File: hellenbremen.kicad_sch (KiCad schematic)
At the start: 5 parts

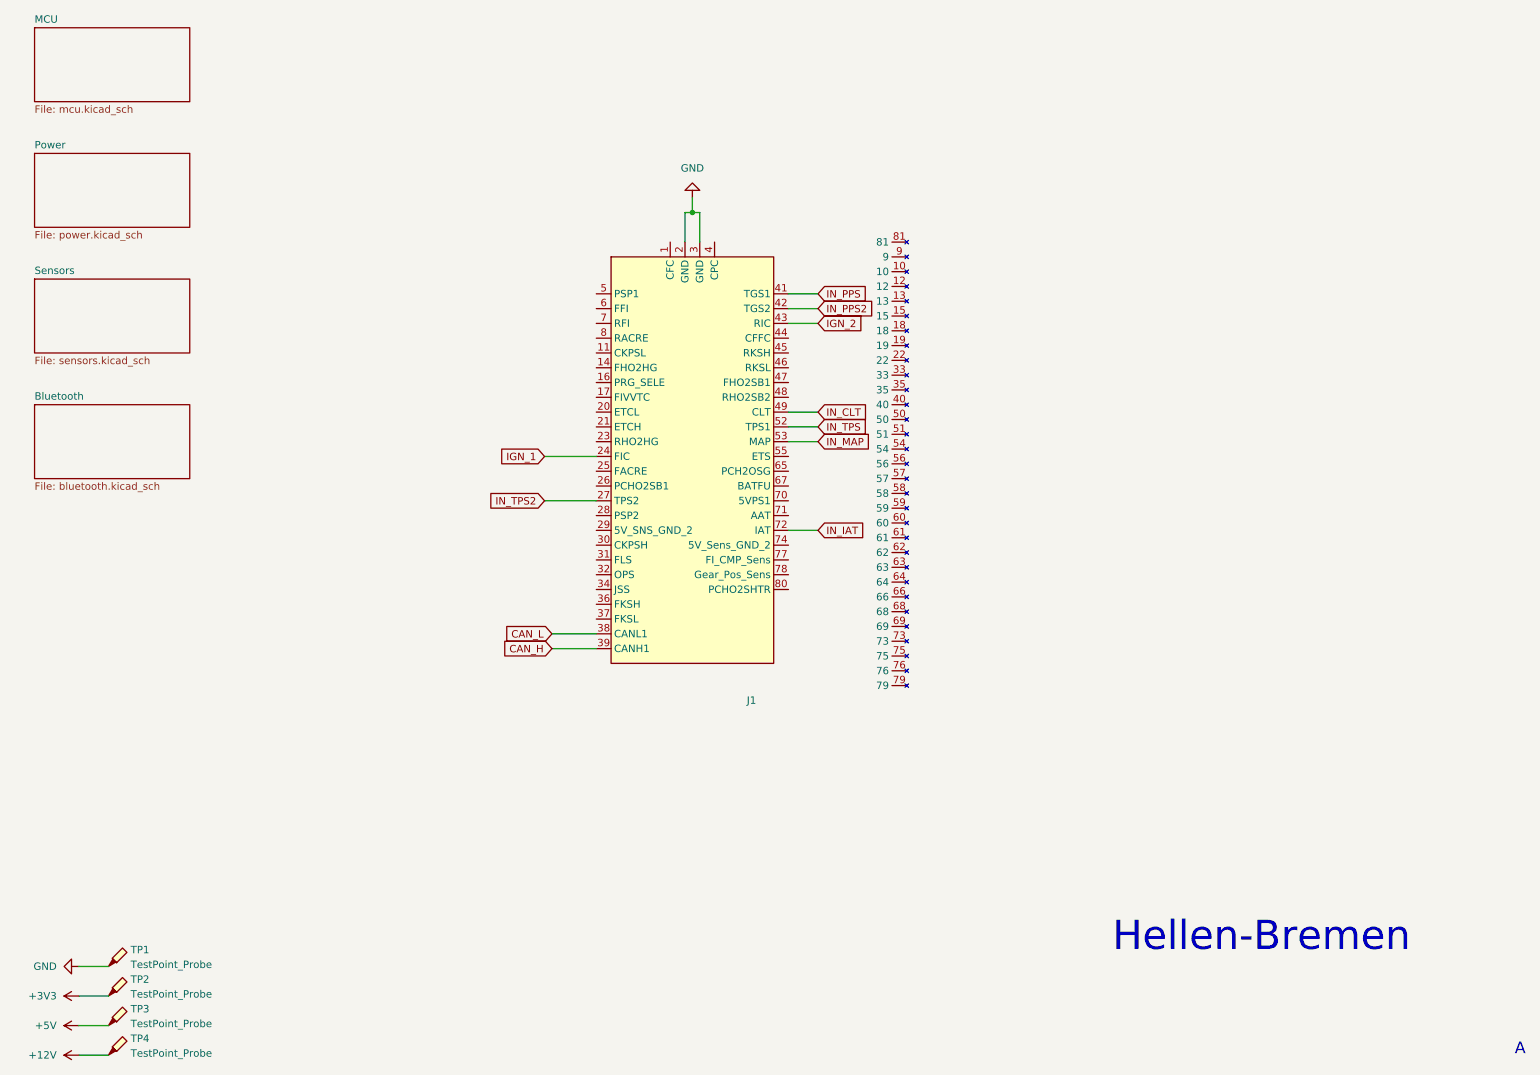
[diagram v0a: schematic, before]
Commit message: Implementing some inputs and outputs
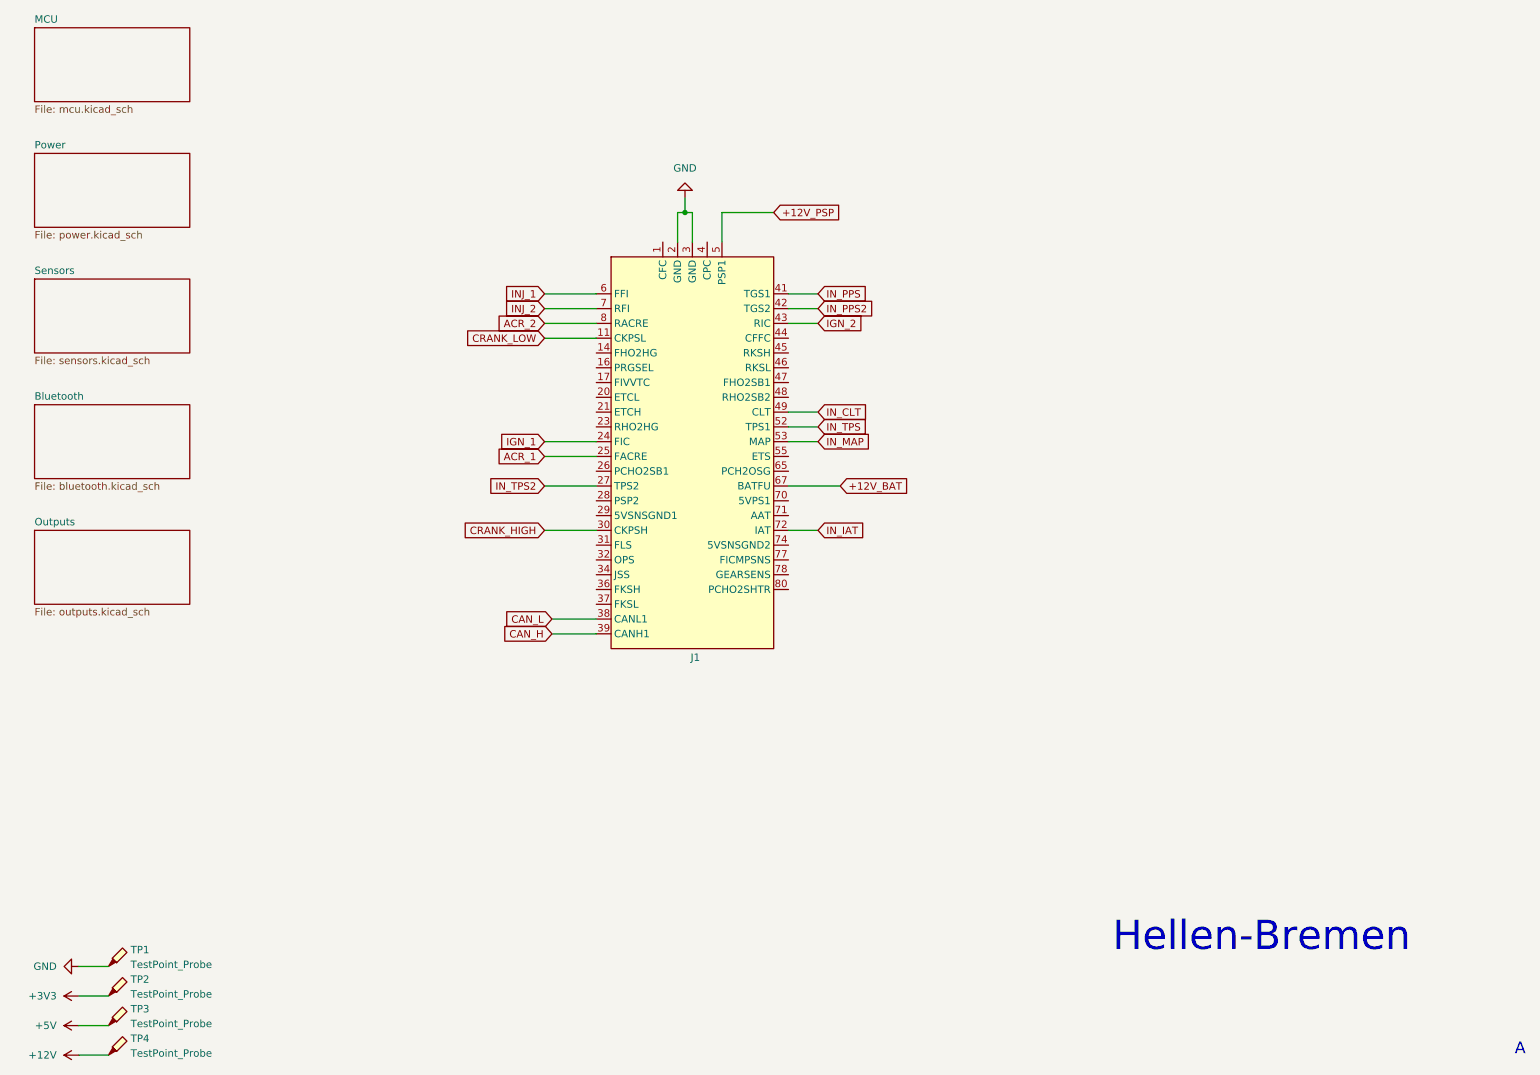
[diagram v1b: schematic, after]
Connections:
- net CRANK_LOW: now reaches J1.11 (CKPSL)
- net ACR_1: now reaches J1.25 (FACRE)
- net CRANK_HIGH: now reaches J1.30 (CKPSH)
- net +12V_PSP: now reaches J1.5 (PSP1)
- net INJ_1: now reaches J1.6 (FFI)
- net +12V_BAT: now reaches J1.67 (BATFU)
- net INJ_2: now reaches J1.7 (RFI)
- net ACR_2: now reaches J1.8 (RACRE)
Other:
- added sheet Outputs (outputs.kicad_sch)

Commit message: still initial layout
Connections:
- net GND: now also J1.29 (5VSNSGND1), J1.74 (5VSNSGND2)
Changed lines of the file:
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@@
 	(wire
 		(pts
-			(xy 144.78 104.14) (xy 149.86 104.14)
+			(xy 144.78 104.14) (xy 153.67 104.14)
 		)
 		(stroke
@@
 	(wire
 		(pts
-			(xy 144.78 63.5) (xy 149.86 63.5)
+			(xy 144.78 63.5) (xy 153.67 63.5)
 		)
 		(stroke
@@
 	(wire
 		(pts
-			(xy 144.78 83.82) (xy 149.86 83.82)
+			(xy 148.59 106.68) (xy 144.78 106.68)
+		)
+		(stroke
+			(width 0)
+			(type default)
+		)
+	)
+	(wire
+		(pts
+			(xy 144.78 83.82) (xy 153.67 83.82)
 		)
 		(stroke
@@
 	(wire
 		(pts
-			(xy 144.78 68.58) (xy 149.86 68.58)
-		)
-		(stroke
-			(width 0)
-			(type default)
-		)
-	)
-	(wire
-		(pts
-			(xy 144.78 88.9) (xy 149.86 88.9)
+			(xy 107.95 101.6) (xy 111.76 101.6)
+		)
+		(stroke
+			(width 0)
+			(type default)
+		)
+	)
+	(wire
+		(pts
+			(xy 144.78 68.58) (xy 153.67 68.58)
+		)
+		(stroke
+			(width 0)
+			(type default)
+		)
+	)
+	(wire
+		(pts
+			(xy 144.78 88.9) (xy 153.67 88.9)
 		)
 		(stroke
@@
 	(wire
 		(pts
-			(xy 144.78 66.04) (xy 149.86 66.04)
-		)
-		(stroke
-			(width 0)
-			(type default)
-		)
-	)
-	(wire
-		(pts
-			(xy 144.78 86.36) (xy 149.86 86.36)
+			(xy 144.78 66.04) (xy 153.67 66.04)
+		)
+		(stroke
+			(width 0)
+			(type default)
+		)
+	)
+	(wire
+		(pts
+			(xy 144.78 86.36) (xy 153.67 86.36)
 		)
 		(stroke
@@
 	(global_label "IN_PPS2"
 		(shape input)
-		(at 149.86 66.04 0)
+		(at 153.67 66.04 0)
 		(fields_autoplaced yes)
 		(effects
@@
 		)
 		(property "Intersheetrefs" "${INTERSHEET_REFS}"
-			(at 160.7071 66.04 0)
+			(at 164.5171 66.04 0)
 			(effects
 				(font
@@
 	(global_label "IN_PPS"
 		(shape input)
-		(at 149.86 63.5 0)
+		(at 153.67 63.5 0)
 		(fields_autoplaced yes)
 		(effects
@@
 		)
 		(property "Intersheetrefs" "${INTERSHEET_REFS}"
-			(at 159.4976 63.5 0)
+			(at 163.3076 63.5 0)
 			(effects
 				(font
@@
 	(global_label "IGN_2"
 		(shape input)
-		(at 149.86 68.58 0)
+		(at 153.67 68.58 0)
 		(fields_autoplaced yes)
 		(effects
@@
 		)
 		(property "Intersheetrefs" "${INTERSHEET_REFS}"
-			(at 158.2276 68.58 0)
+			(at 162.0376 68.58 0)
 			(effects
 				(font
@@
 	(global_label "IN_TPS"
 		(shape input)
-		(at 149.86 86.36 0)
+		(at 153.67 86.36 0)
 		(fields_autoplaced yes)
 		(effects
@@
 		)
 		(property "Intersheetrefs" "${INTERSHEET_REFS}"
-			(at 159.1952 86.36 0)
+			(at 163.0052 86.36 0)
 			(effects
 				(font
@@
 	(global_label "IN_CLT"
 		(shape input)
-		(at 149.86 83.82 0)
+		(at 153.67 83.82 0)
 		(fields_autoplaced yes)
 		(effects
@@
 		)
 		(property "Intersheetrefs" "${INTERSHEET_REFS}"
-			(at 159.0138 83.82 0)
+			(at 162.8238 83.82 0)
 			(effects
 				(font
@@
 	(global_label "IN_IAT"
 		(shape input)
-		(at 149.86 104.14 0)
+		(at 153.67 104.14 0)
 		(fields_autoplaced yes)
 		(effects
@@
 		)
 		(property "Intersheetrefs" "${INTERSHEET_REFS}"
-			(at 158.4091 104.14 0)
+			(at 162.2191 104.14 0)
 			(effects
 				(font
@@
 	(global_label "IN_MAP"
 		(shape input)
-		(at 149.86 88.9 0)
+		(at 153.67 88.9 0)
 		(fields_autoplaced yes)
 		(effects
@@
 		)
 		(property "Intersheetrefs" "${INTERSHEET_REFS}"
-			(at 159.5581 88.9 0)
+			(at 163.3681 88.9 0)
 			(effects
 				(font
@@
 	(symbol
 		(lib_id "power:GND")
+		(at 148.59 106.68 90)
+		(unit 1)
+		(exclude_from_sim no)
+		(in_bom yes)
+		(on_board yes)
+		(dnp no)
+		(fields_autoplaced yes)
+		(property "Reference" "#PWR039"
+			(at 154.94 106.68 0)
+			(effects
+				(font
+					(size 1.27 1.27)
+				)
+				(hide yes)
+			)
+		)
+		(property "Value" "GND"
+			(at 152.4 106.6801 90)
+			(effects
+				(font
+					(size 1.27 1.27)
+				)
+				(justify right)
+			)
+		)
+		(property "Footprint" ""
+			(at 148.59 106.68 0)
+			(effects
+				(font
+					(size 1.27 1.27)
+				)
+				(hide yes)
+			)
+		)
+		(property "Datasheet" ""
+			(at 148.59 106.68 0)
+			(effects
+				(font
+					(size 1.27 1.27)
+				)
+				(hide yes)
+			)
+		)
+		(property "Description" "Power symbol creates a global label with name \"GND\" , ground"
+			(at 148.59 106.68 0)
+			(effects
+				(font
+					(size 1.27 1.27)
+				)
+				(hide yes)
+			)
+		)
+		(pin "1"
+		)
+		(instances
+			(project "hellenbremen"
+				(path "/83409e39-90d0-4c85-be2e-bd292bea7c12"
+					(reference "#PWR039")
+					(unit 1)
+				)
+			)
+		)
+	)
+	(symbol
+		(lib_id "power:GND")
 		(at 22.86 179.07 270)
 		(unit 1)
@@
 					(unit 1)
 				)
+			)
+		)
+	)
+	(symbol
+		(lib_id "power:GND")
+		(at 107.95 101.6 270)
+		(unit 1)
+		(exclude_from_sim no)
+		(in_bom yes)
+		(on_board yes)
+		(dnp no)
+		(fields_autoplaced yes)
+		(property "Reference" "#PWR038"
+			(at 101.6 101.6 0)
+			(effects
+				(font
+					(size 1.27 1.27)
+				)
+				(hide yes)
+			)
+		)
+		(property "Value" "GND"
+			(at 104.14 101.5999 90)
+			(effects
+				(font
+					(size 1.27 1.27)
+				)
+				(justify right)
+			)
+		)
+		(property "Footprint" ""
+			(at 107.95 101.6 0)
+			(effects
+				(font
+					(size 1.27 1.27)
+				)
+				(hide yes)
+			)
+		)
+		(property "Datasheet" ""
+			(at 107.95 101.6 0)
+			(effects
+				(font
+					(size 1.27 1.27)
+				)
+				(hide yes)
+			)
+		)
+		(property "Description" "Power symbol creates a global label with name \"GND\" , ground"
+			(at 107.95 101.6 0)
+			(effects
+				(font
+					(size 1.27 1.27)
+				)
+				(hide yes)
+			)
+		)
+		(pin "1"
+		)
+		(instances
+			(project "hellenbremen"
+				(path "/83409e39-90d0-4c85-be2e-bd292bea7c12"
+					(reference "#PWR038")
+					(unit 1)
+				)

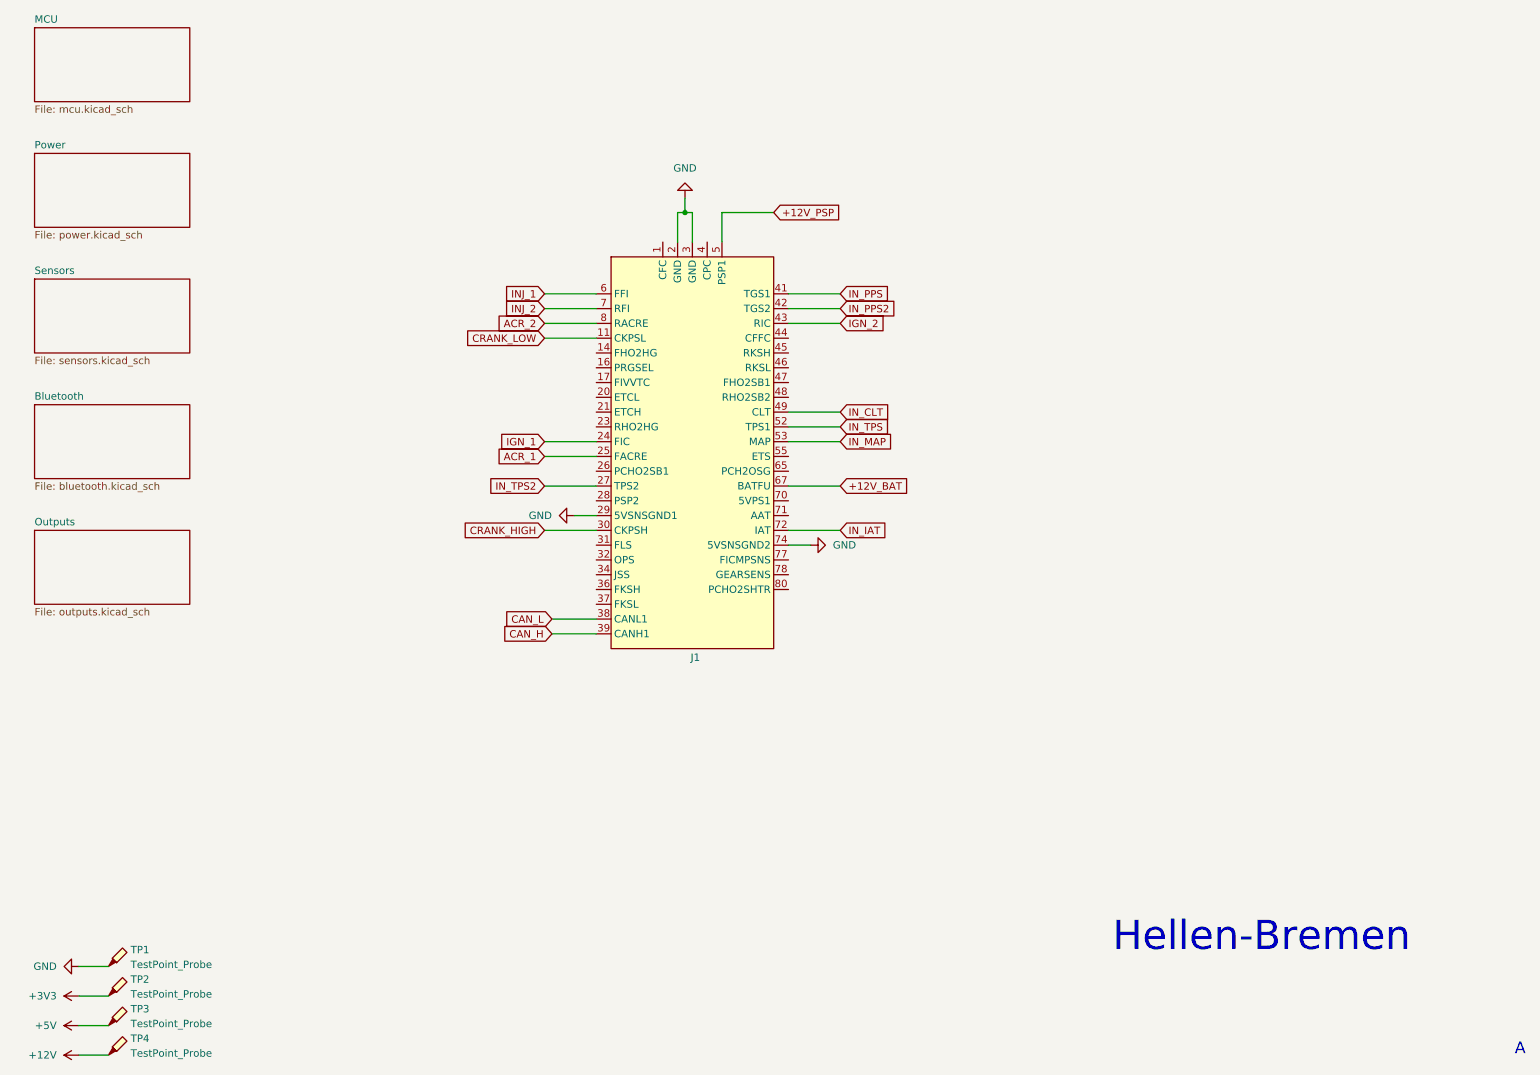
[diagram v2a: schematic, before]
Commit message: igntion igbt, cooling mosfet
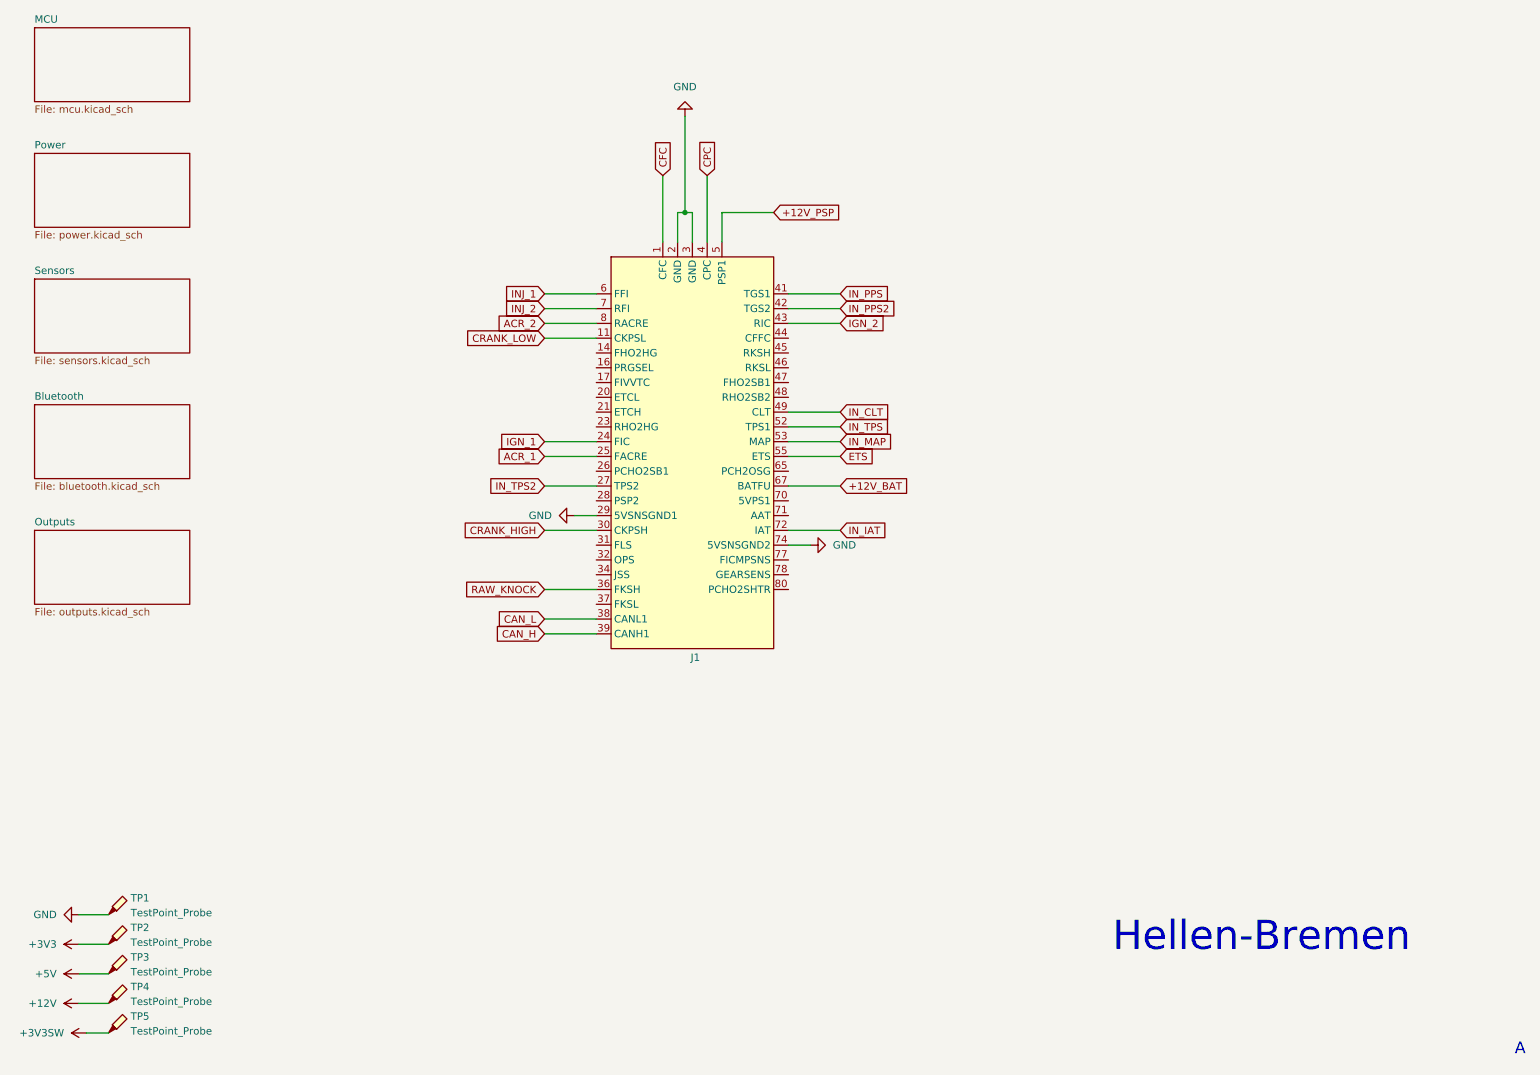
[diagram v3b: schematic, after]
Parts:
- added TP5: TestPoint_Probe, TestPoint:TestPoint_Pad_D2.0mm, symbol Connector:TestPoint_Probe
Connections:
- net CFC: now reaches J1.1 (CFC)
- net RAW_KNOCK: now reaches J1.36 (FKSH)
- net CPC: now reaches J1.4 (CPC)
- net ETS: now reaches J1.55 (ETS)
- new net +3V3SW: TP5.1
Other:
- moved on the sheet: TP1, TP2, TP3, TP4

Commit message: trying out a layout and routing
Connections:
- net GND: now also J1.14 (FHO2HG), J1.23 (RHO2HG), J1.65 (PCH2OSG)
- net H2OSPC: now reaches J1.26 (PCHO2SB1)
- net IN_JSS: now reaches J1.34 (JSS)
- net RAW_KNOCK_R: now reaches J1.45 (RKSH)
- net H2OS1: now reaches J1.47 (FHO2SB1)
- net H2OS2: now reaches J1.48 (RHO2SB2)
- net IN_AAT: now reaches J1.71 (AAT)
- net RAW_KNOCK renamed RAW_KNOCK_F

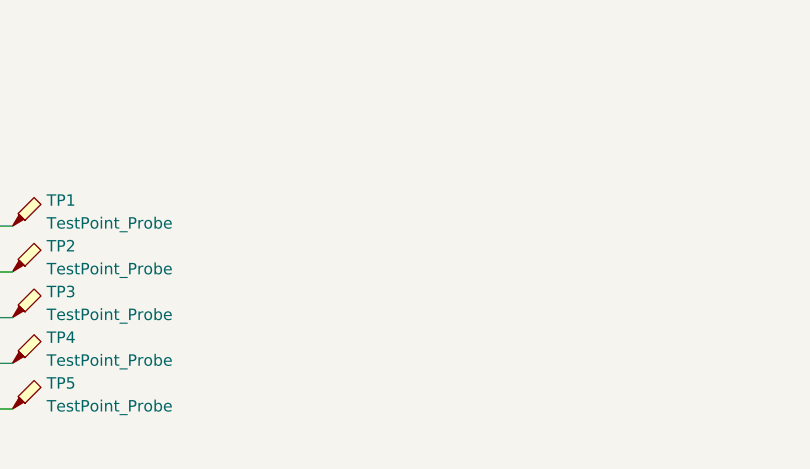
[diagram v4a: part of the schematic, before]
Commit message: Fiducial Marks and Via Stitching
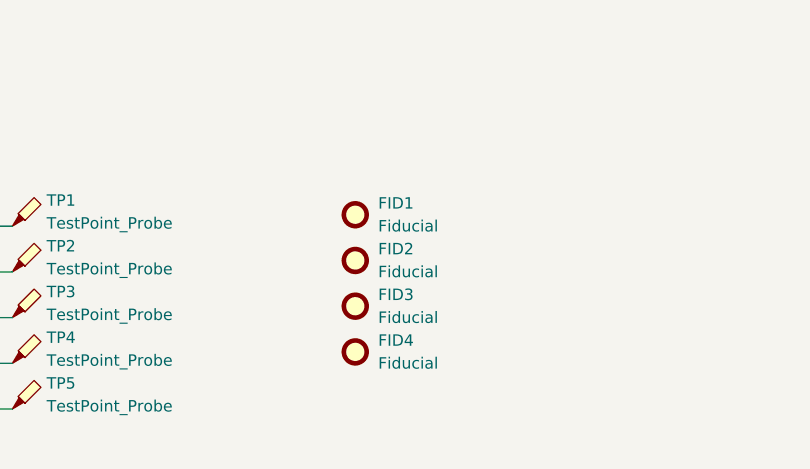
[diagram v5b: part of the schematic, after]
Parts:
- added FID1, FID2, FID3, FID4: Fiducial, Fiducial:Fiducial_1mm_Mask2mm, symbol Mechanical:Fiducial
- J1: now left out of the parts list
